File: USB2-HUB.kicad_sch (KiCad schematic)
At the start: 32 parts, among them J11 USB_OTG, J13 690-008-221-904, J14 Conn_02x05_Odd_Even, U13 FSUSB42MUX, U4 TPD4EUSB30, U6 USB2514B-I/M2, U7 AP22653W6, Y1 24MHz

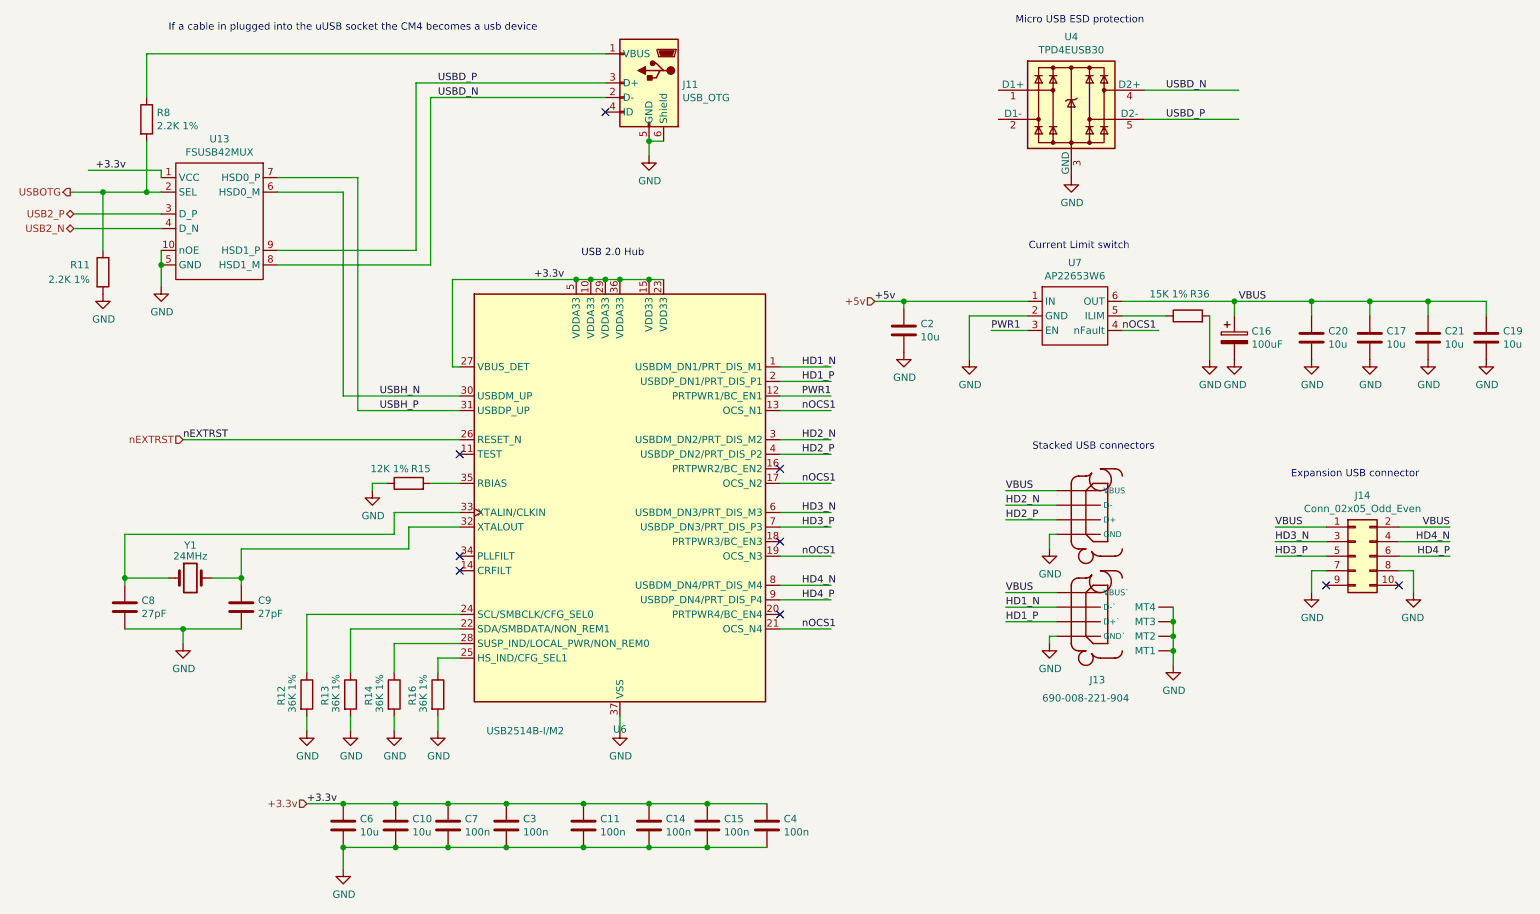
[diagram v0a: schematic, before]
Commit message: removed many unused parts
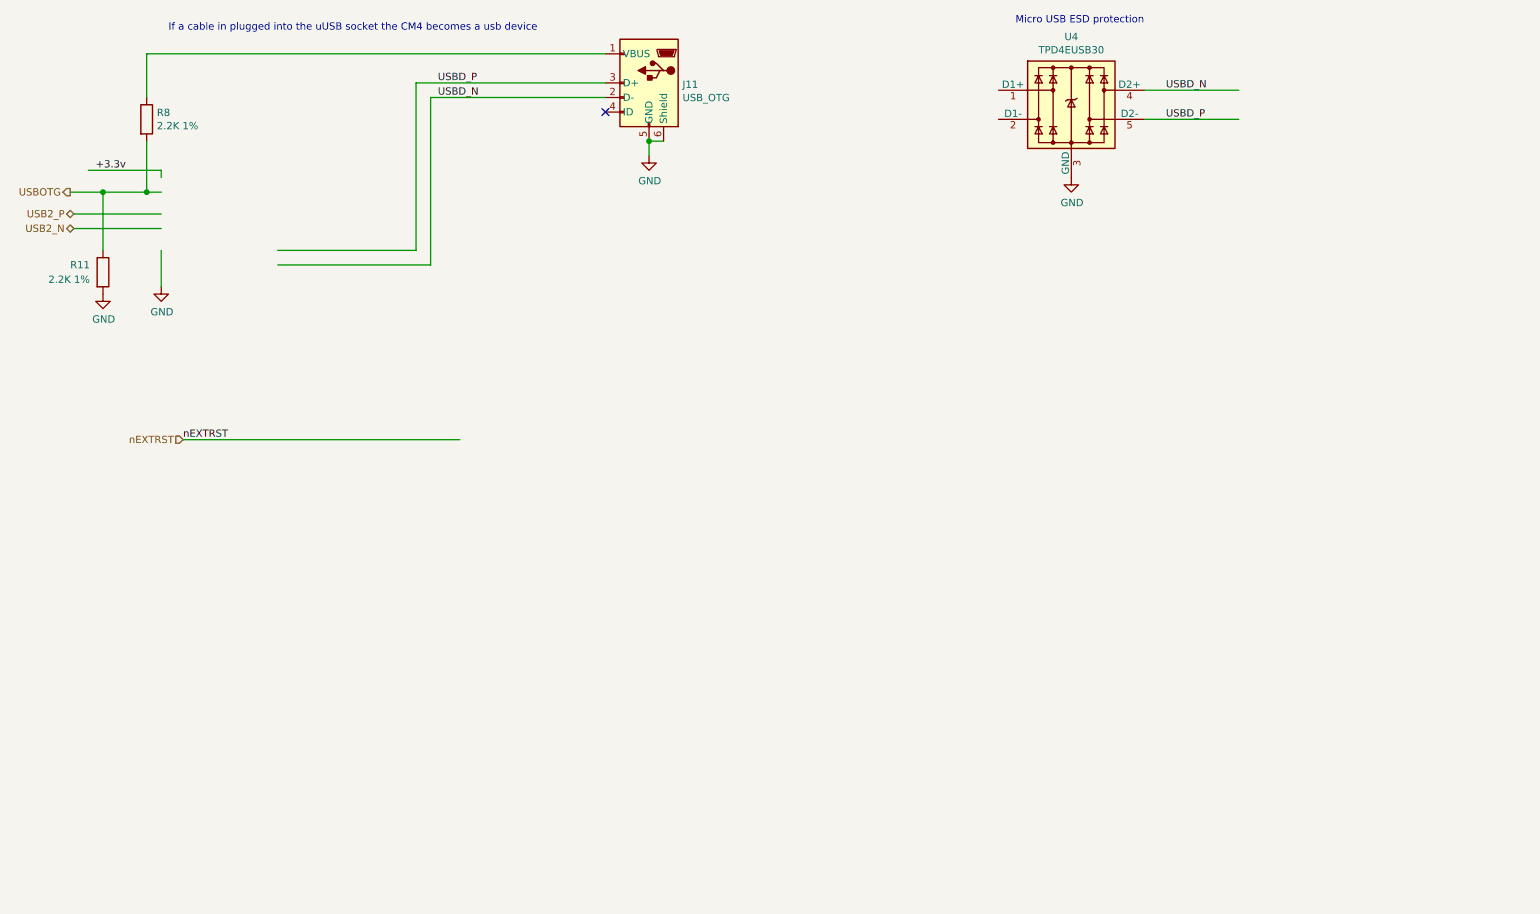
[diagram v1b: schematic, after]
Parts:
- removed C10, C17, C19, C2, C20, C21, C6: 10u, Capacitor_SMD:C_0805_2012Metric, symbol Device:C
- removed C11, C14, C15, C3, C4, C7: 100n, Capacitor_SMD:C_0402_1005Metric, symbol Device:C
- removed C16: 100uF, Capacitor_Tantalum_SMD:CP_EIA-7343-31_Kemet-D, symbol Device:CP
- removed C8, C9: 27pF, Capacitor_SMD:C_0402_1005Metric, symbol Device:C
- removed J13: 690-008-221-904, CM4IO:MOLEX_USB_67298-4090, symbol CM4IO:USB_67298-4090
- removed J14: Conn_02x05_Odd_Even, Connector_PinHeader_2.54mm:PinHeader_2x05_P2.54mm_Vertical, symbol Connector_Generic:Conn_02x05_Odd_Even
- removed R12, R13, R14, R16: 36K 1%, Resistor_SMD:R_0402_1005Metric, symbol Device:R
- removed R15: 12K 1%, Resistor_SMD:R_0402_1005Metric, symbol Device:R
- removed R36: 15K 1%, Resistor_SMD:R_0402_1005Metric, symbol Device:R
- removed U13: FSUSB42MUX, Package_SO:MSOP-10_3x3mm_P0.5mm, symbol CM4IO:FSUSB42MX
- removed U6: USB2514B-I/M2, Package_DFN_QFN:QFN-36-1EP_6x6mm_P0.5mm_EP3.7x3.7mm, symbol Interface_USB:USB2514B_Bi
- removed U7: AP22653W6, Package_TO_SOT_SMD:SOT-23-6, symbol CM4IO:AP2553W6
- removed Y1: 24MHz, Crystal:Crystal_SMD_HC49-SD, symbol Device:Crystal
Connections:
- no-connect marks 9 -> 1
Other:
- note removed: "Current Limit switch"
- note removed: "Expansion USB connector"
- note removed: "Stacked USB connectors"
- note removed: "USB 2.0 Hub"
- company: © 2020-2022 Raspberry Pi Ltd (formerly Raspberry Pi (Trading) Ltd.) -> (none)
- title: Compute Module 4 IO Board - USB -> bitcart - USB

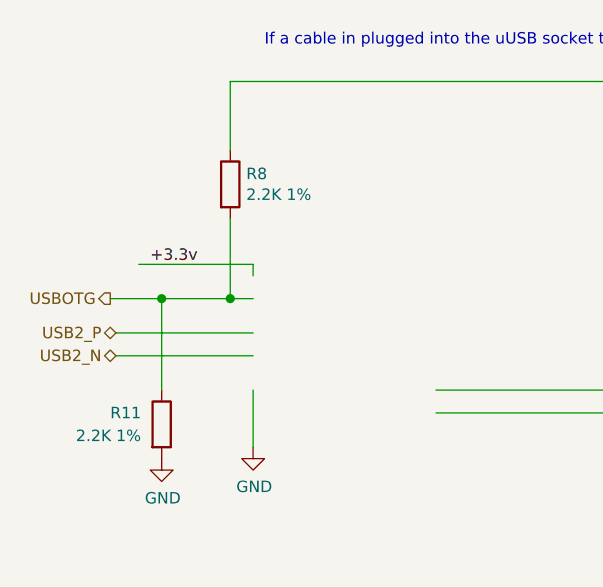
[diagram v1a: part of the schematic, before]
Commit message: changed PoE transformer to Wurth 7491194912
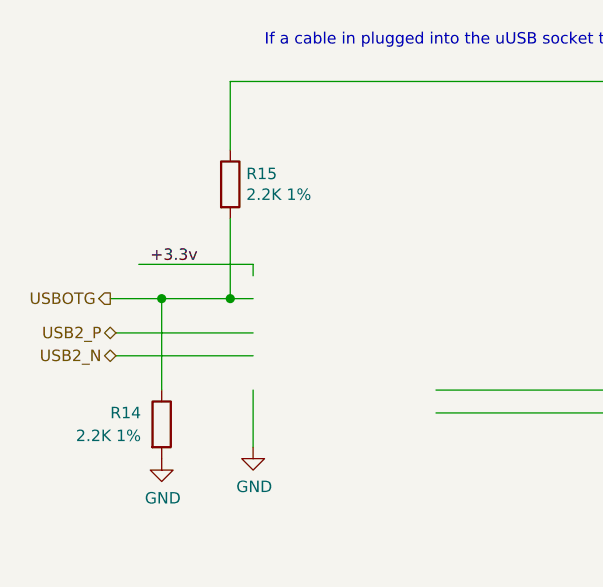
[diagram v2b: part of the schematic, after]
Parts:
- renumbered R11 to R14, R8 to R15
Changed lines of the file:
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@@
   (symbol (lib_id "Device:R") (at 40.64 45.72 0) (unit 1)
     (in_bom yes) (on_board yes)
-    (property "Reference" "R8" (id 0) (at 42.418 44.5516 0)
+    (property "Reference" "R15" (id 0) (at 42.418 44.5516 0)
       (effects (font (size 1.27 1.27)) (justify left))
     )
@@
   (symbol (lib_id "Device:R") (at 33.02 72.39 0) (unit 1)
     (in_bom yes) (on_board yes)
-    (property "Reference" "R11" (id 0) (at 27.305 71.12 0)
+    (property "Reference" "R14" (id 0) (at 27.305 71.12 0)
       (effects (font (size 1.27 1.27)) (justify left))
     )

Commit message: started routing PoE
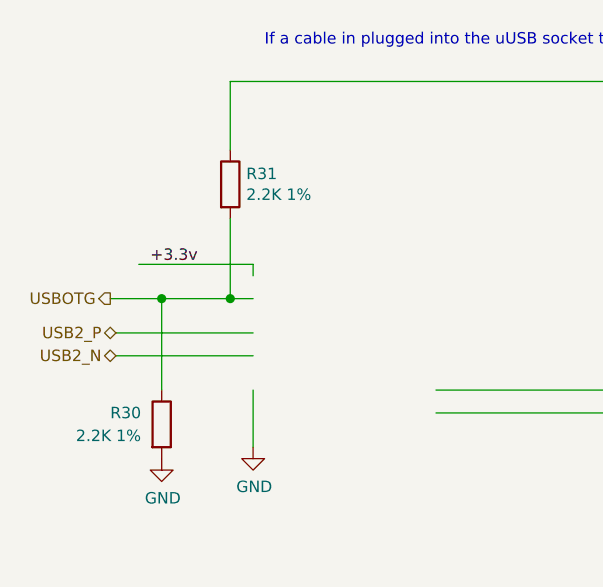
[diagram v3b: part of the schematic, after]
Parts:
- renumbered R14 to R30, R15 to R31
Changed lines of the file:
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@@
   (symbol (lib_id "Device:R") (at 40.64 45.72 0) (unit 1)
     (in_bom yes) (on_board yes)
-    (property "Reference" "R15" (id 0) (at 42.418 44.5516 0)
+    (property "Reference" "R31" (id 0) (at 42.418 44.5516 0)
       (effects (font (size 1.27 1.27)) (justify left))
     )
@@
   (symbol (lib_id "Device:R") (at 33.02 72.39 0) (unit 1)
     (in_bom yes) (on_board yes)
-    (property "Reference" "R14" (id 0) (at 27.305 71.12 0)
+    (property "Reference" "R30" (id 0) (at 27.305 71.12 0)
       (effects (font (size 1.27 1.27)) (justify left))
     )
